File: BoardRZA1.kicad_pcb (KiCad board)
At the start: 4 copper layers, 99.9 x 80 mm, 153 parts, among them CON1 USB-MINI-B, CON2 USB-A-PCB, CON3 microSD, CON4 BARREL_JACK, J1 HR911105A, J2 SIL38, P1 JTAG, SW1 RESET, SW2 NMI, SW3 SW0, SW4 SW1, U1 RZ-A1L, U2 13MHz, U3 48MHz, U4 N25QXXX, U5 AS4C16M16S, U6 BA3259HFP, U7 BU42xx, U8 KSZ8041MLL, U9 25MHz, X1 32.768k

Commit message: Logo & move some nets
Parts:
- added SYM: Symbol_OSHW-Logo_CopperTop_07Jul2012, Symbols:Symbol_OSHW-Logo_CopperTop, F.Cu at (28.5, 79.1)
- added SYM: Symbol_OSHW-Logo_CopperTop_07Jul2012, Symbols:Symbol_OSHW-Logo_CopperTop, B.Cu at (103.0, 86.1)
- added Sym: Symbol_ESD-Logo_CopperTop_21Apr2011, Symbols:Symbol_ESD-Logo_CopperTop, F.Cu at (31.3, 72.3)
- added Sym: Symbol_CreativeCommons_Typ2_CopperTop_Small, Symbols:Symbol_CreativeCommons_CopperTop_Type2_Small, F.Cu at (34.3, 79.1)
- added Sym: Symbol_CreativeCommons_Typ2_CopperTop_Small, Symbols:Symbol_CreativeCommons_CopperTop_Type2_Small, B.Cu at (96.9, 86.0)
- added Sym: Symbol_ESD-Logo_CopperTop_21Apr2011, Symbols:Symbol_ESD-Logo_CopperTop, B.Cu at (99.8, 78.4)
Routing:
- net VSS: track 590.2 -> 559.9 mm, vias 38 -> 41
- net Net-(CON1-Pad1): track 51.0 -> 60.8 mm
- net /ET_TXD2: track 82.8 -> 84.7 mm
- net /ET_TXD1: track 82.0 -> 83.9 mm
- net /ET_TXD0: track 83.0 -> 85.0 mm
- net /ET_TXD3: track 85.3 -> 87.2 mm
- net /ET_TXCLK: track 68.1 -> 70.0 mm
- net /P6_8: track 117.9 -> 116.7 mm
- net /SW0: track 43.9 -> 42.7 mm
- net /P6_7: track 128.6 -> 127.5 mm
- added copper zone on B.Cu, net /ET_1v8

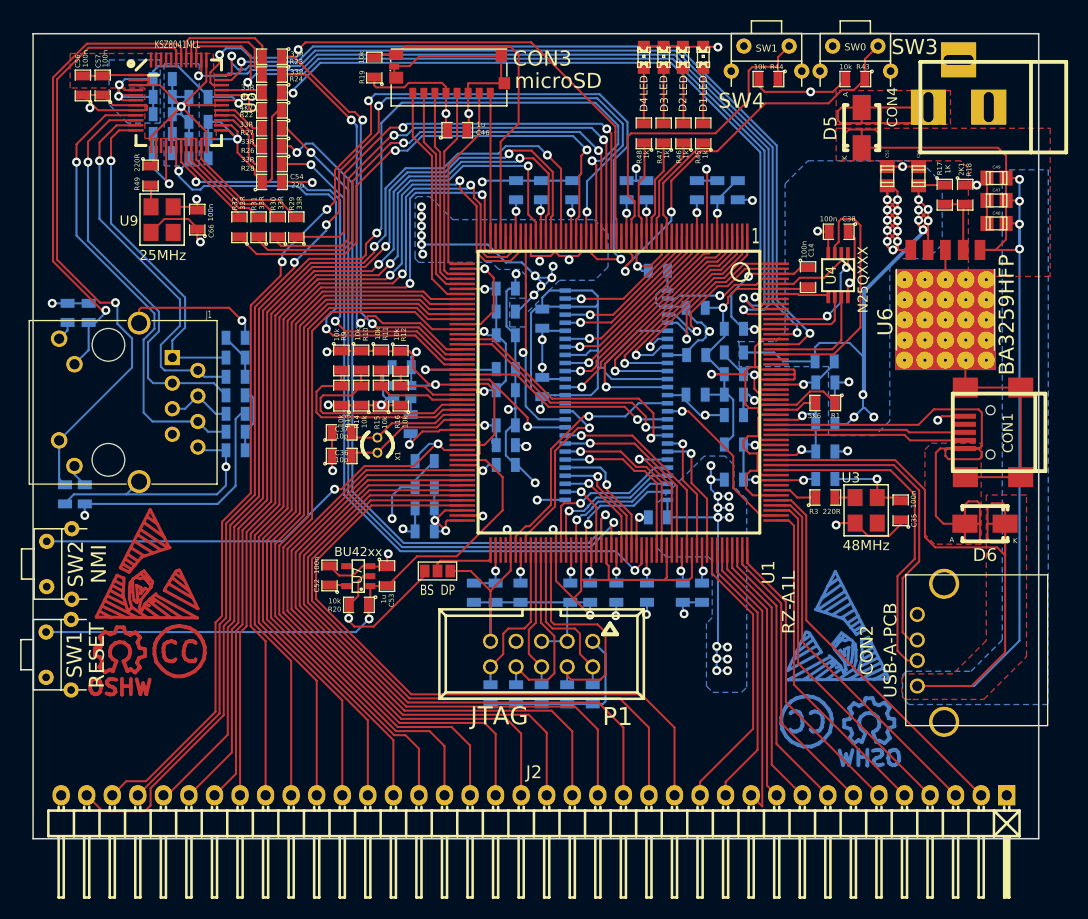
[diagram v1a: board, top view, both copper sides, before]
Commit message: PHY OSC to XI fixed. Move some refs. Optional pulldown on TRST
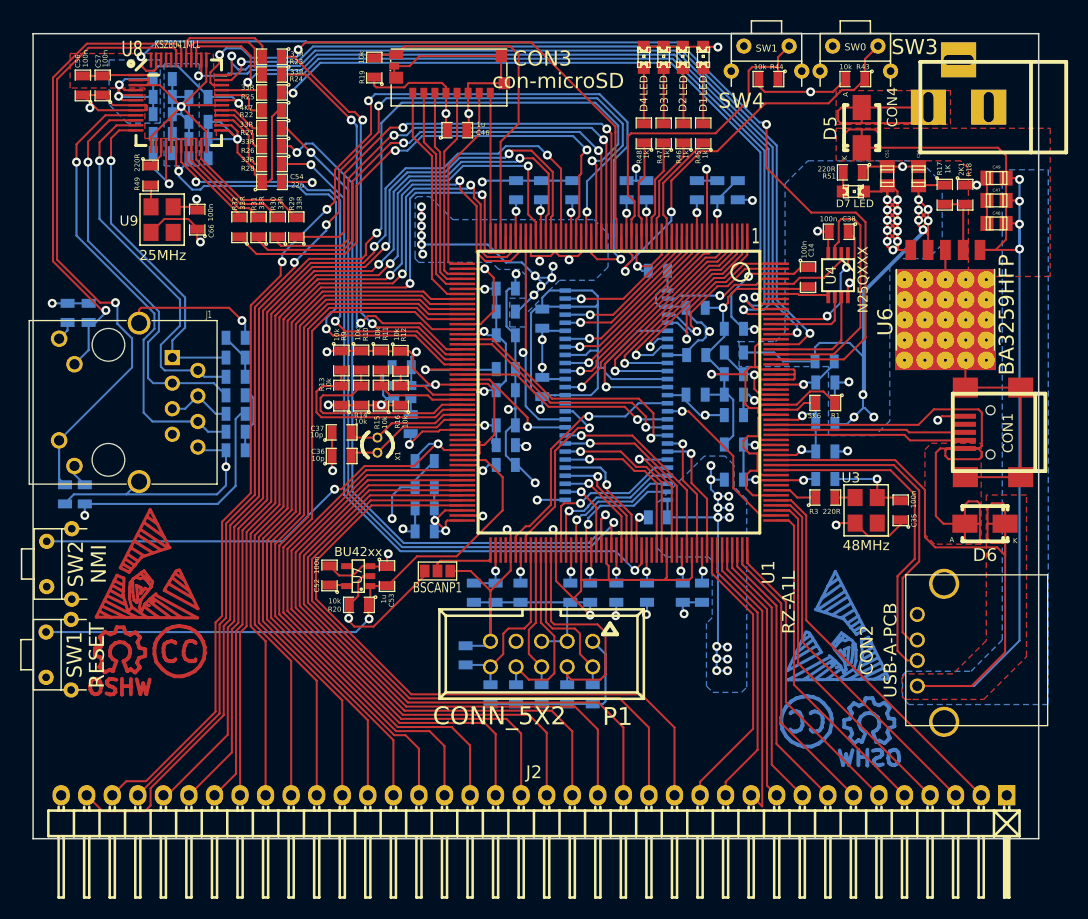
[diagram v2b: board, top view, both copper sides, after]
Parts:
- removed BS  DP: GS3, Connect:GS3
- added BSCANP1: GS3, Connect:GS3, F.Cu at (60.1, 71.0)
- added D7: LED, LEDs:LED-0805, F.Cu at (101.4, 33.3)
- added R50: 10k, SMD_Packages:SM0805, B.Cu at (62.9, 79.4)
- added R51: 220R, SMD_Packages:SM0805, F.Cu at (101.3, 31.4)
- CON3: value microSD -> con-microSD
- P1: value JTAG -> CONN_5X2
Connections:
- U1 pad 189: Net-(U1-Pad189) -> /PHY_RESET
- U8 pad 14: /ETH_CLK -> Net-(U8-Pad14)
- U8 pad 15: Net-(U8-Pad15) -> /ETH_CLK
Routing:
- net /PHY_RESET: track 0.00 -> 107.5 mm, vias 0 -> 2
- net VSS: track 559.9 -> 565.2 mm
- net /JTAG_TRST: track 16.0 -> 18.5 mm
- net +3.3V: track 317.7 -> 320.2 mm
- net Net-(D7-Pad1): track 0.00 -> 1.92 mm

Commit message: Add 10uF decouple on pvcc, vcc & 3v3
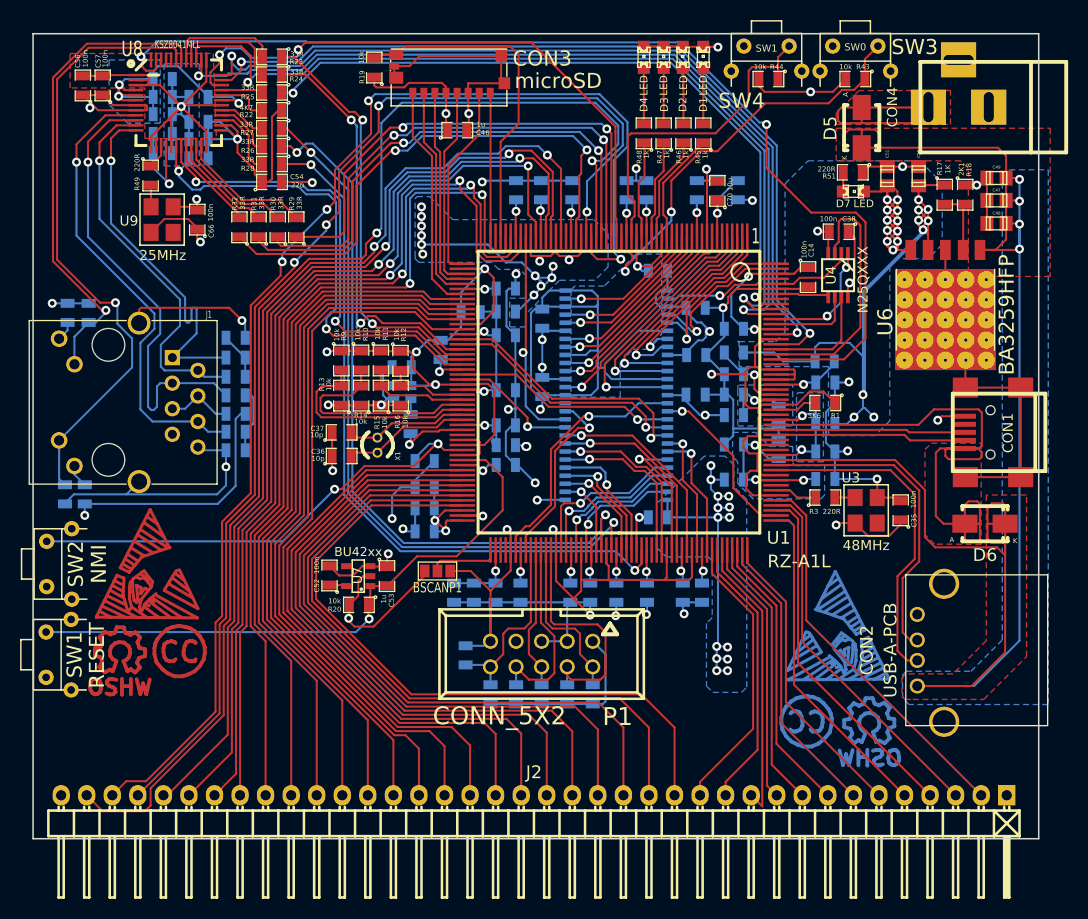
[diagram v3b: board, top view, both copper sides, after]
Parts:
- added C67: 10u, SMD_Packages:SM0805, B.Cu at (94.0, 55.6)
- added C68: 10u, SMD_Packages:SM0805, B.Cu at (94.0, 58.9)
- added C69: 10u, SMD_Packages:SM0805, B.Cu at (63.4, 45.3)
- added C70: 10u, SMD_Packages:SM0805, F.Cu at (87.9, 33.2)
- added C71: 10u, SMD_Packages:SM0805, B.Cu at (61.7, 73.2)
- CON3: value con-microSD -> microSD
- moved C17 6.75 mm to (60.4, 49.0), turned to 90 degrees
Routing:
- net VSS: track 565.2 -> 594.8 mm
- net /VCC: track 131.8 -> 126.0 mm
- net Net-(J1-Pad3): track 41.5 -> 46.7 mm
- net Net-(J1-Pad1): track 33.5 -> 37.6 mm
- net /USBDPVCC: track 14.0 -> 16.9 mm
- net /PVCC: track 176.3 -> 179.1 mm
- net /USBAPVCC: track 5.54 -> 8.19 mm
- added copper zone on B.Cu, net /USBAPVCC
- added copper zone on B.Cu, net /USBDPVCC
- added copper zone on B.Cu, net /USBDVCC

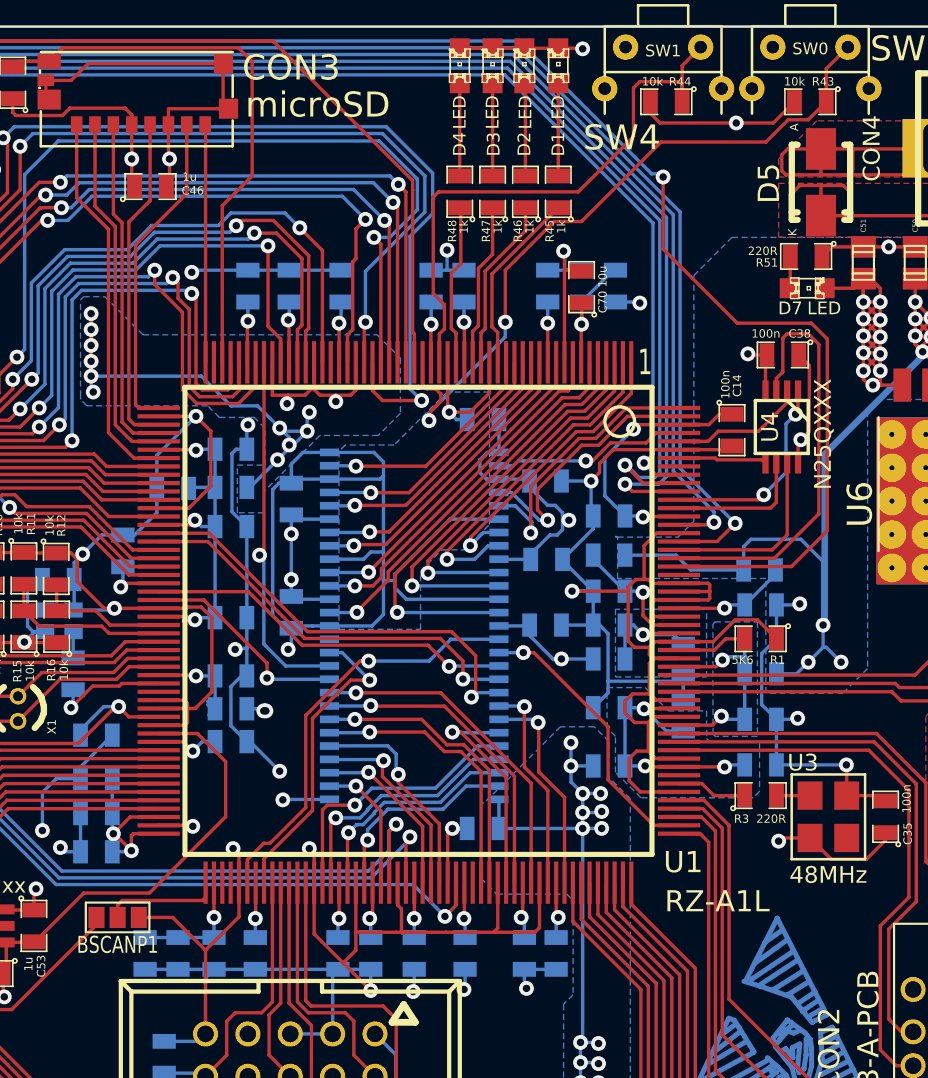
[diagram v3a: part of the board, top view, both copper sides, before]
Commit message: Add 100pF C over power rails (700MHz filters) ERC pass DRC pass
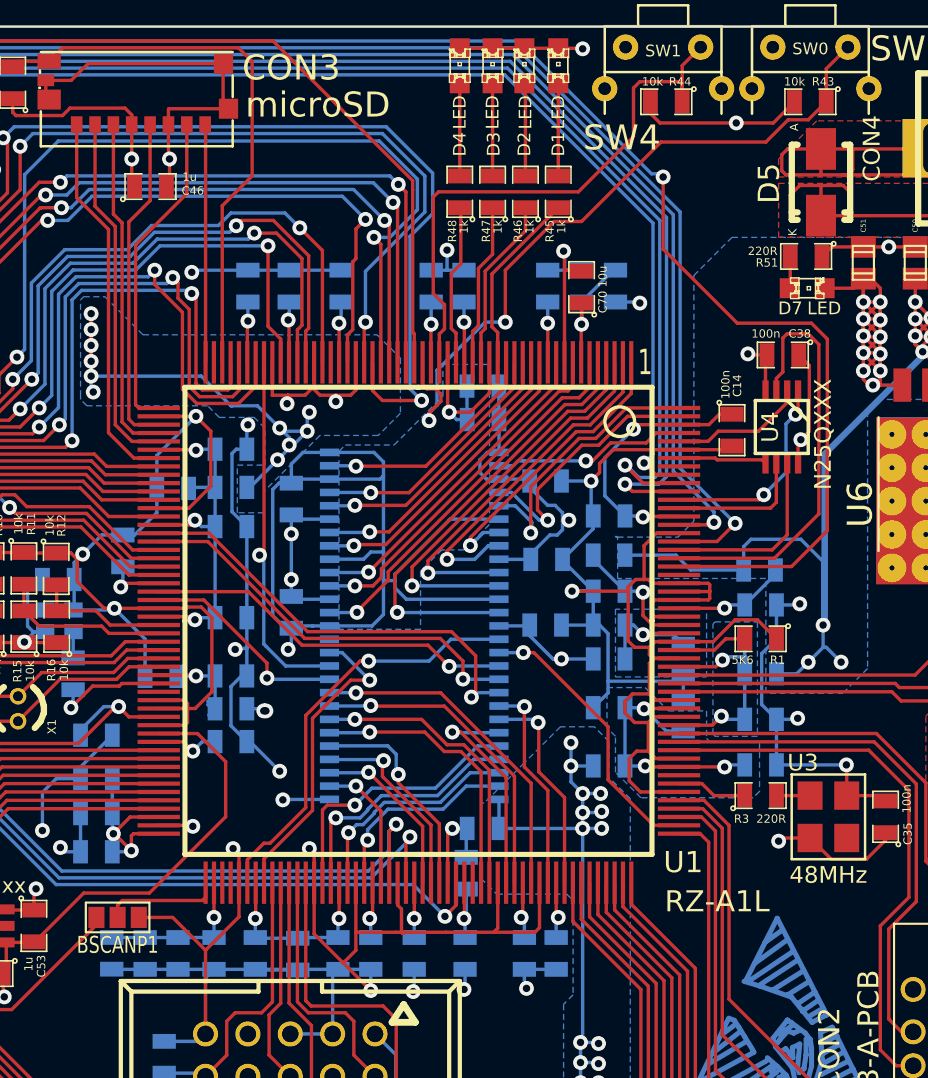
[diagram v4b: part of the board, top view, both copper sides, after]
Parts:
- added C72: 100p, SMD_Packages:SM0805, B.Cu at (82.0, 39.1)
- added C73: 100p, SMD_Packages:SM0805, B.Cu at (81.0, 68.3)
- added C74: 100p, SMD_Packages:SM0805, B.Cu at (59.7, 73.1)
- added C75: 100p, SMD_Packages:SM0805, B.Cu at (70.9, 73.2)
- added C76: 100p, SMD_Packages:SM0805, B.Cu at (62.7, 56.5)
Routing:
- net VSS: track 594.8 -> 608.0 mm
- net /VCC: track 126.0 -> 131.0 mm
- net /PVCC: track 179.1 -> 183.0 mm
- net +3.3V: track 320.2 -> 322.2 mm
- net /PLLVCC: track 7.62 -> 8.78 mm
- net /SW0: track 42.7 -> 43.4 mm

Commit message: Arrangue PCB
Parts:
- moved R20 9.11 mm to (60.9, 71.4), turned to 90 degrees
- moved C52 7.15 mm to (55.9, 68.6), turned to 0 degrees
- moved BSCANP1 4.47 mm to (64.1, 73.0)
- moved SYM 4.31 mm to (100.1, 82.9)
- moved C53 3.87 mm to (58.9, 71.4)
- moved Sym 3.85 mm to (94.8, 82.8)
- moved U7 3.68 mm to (55.9, 71.3)
- moved Sym 3.56 mm to (97.0, 76.3)
- moved SYM 3.51 mm to (31.7, 77.6)
- moved Sym 3.44 mm to (34.5, 71.0)
- moved Sym 3.30 mm to (37.3, 77.6)
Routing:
- net VSS: track 608.0 -> 600.6 mm, vias 41 -> 40
- net /P1_13: track 65.6 -> 59.4 mm
- net /P1_10: track 61.3 -> 55.2 mm
- net /P1_9: track 60.0 -> 53.8 mm
- net /P1_15: track 68.3 -> 62.1 mm
- net /P1_14: track 66.9 -> 60.7 mm
- net /P1_11: track 62.7 -> 56.6 mm
- net /P1_8: track 58.6 -> 52.4 mm
- net /P1_12: track 64.2 -> 58.0 mm
- net +3.3V: track 322.2 -> 327.8 mm, vias 54 -> 53
- net /P1_0: track 28.2 -> 24.9 mm
- net Net-(C52-Pad1): track 1.70 -> 4.73 mm
- net /P7_9: track 70.2 -> 67.8 mm
- net /P7_8: track 70.0 -> 67.5 mm
- net /P7_10: track 70.5 -> 68.0 mm
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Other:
- board text added: "+3.3v"
- board text added: "GND"
- board text added: "P1.0"
- board text added: "P1.1"
- board text added: "P1.10"
- board text added: "P1.11"
- board text added: "P1.12"
- board text added: "P1.13"
- board text added: "P1.14"
- board text added: "P1.15"
- board text added: "P1.2"
- board text added: "P1.3"
- board text added: "P1.4"
- board text added: "P1.5"
- board text added: "P1.6"
- board text added: "P1.7"
- board text added: "P1.8"
- board text added: "P1.9"
- board text added: "P2.7"
- board text added: "P2.8"
- board text added: "P2.9"
- board text added: "P3.15"
- board text added: "P6.10"
- board text added: "P6.11"
- board text added: "P6.12"
- board text added: "P6.13"
- board text added: "P6.14"
- board text added: "P6.15"
- board text added: "P6.6"
- board text added: "P6.7"
- board text added: "P6.9"
- board text added: "P7.10"
- board text added: "P7.11"
- board text added: "P7.12"
- board text added: "P7.13"
- board text added: "P7.8"
- board text added: "P7.9"

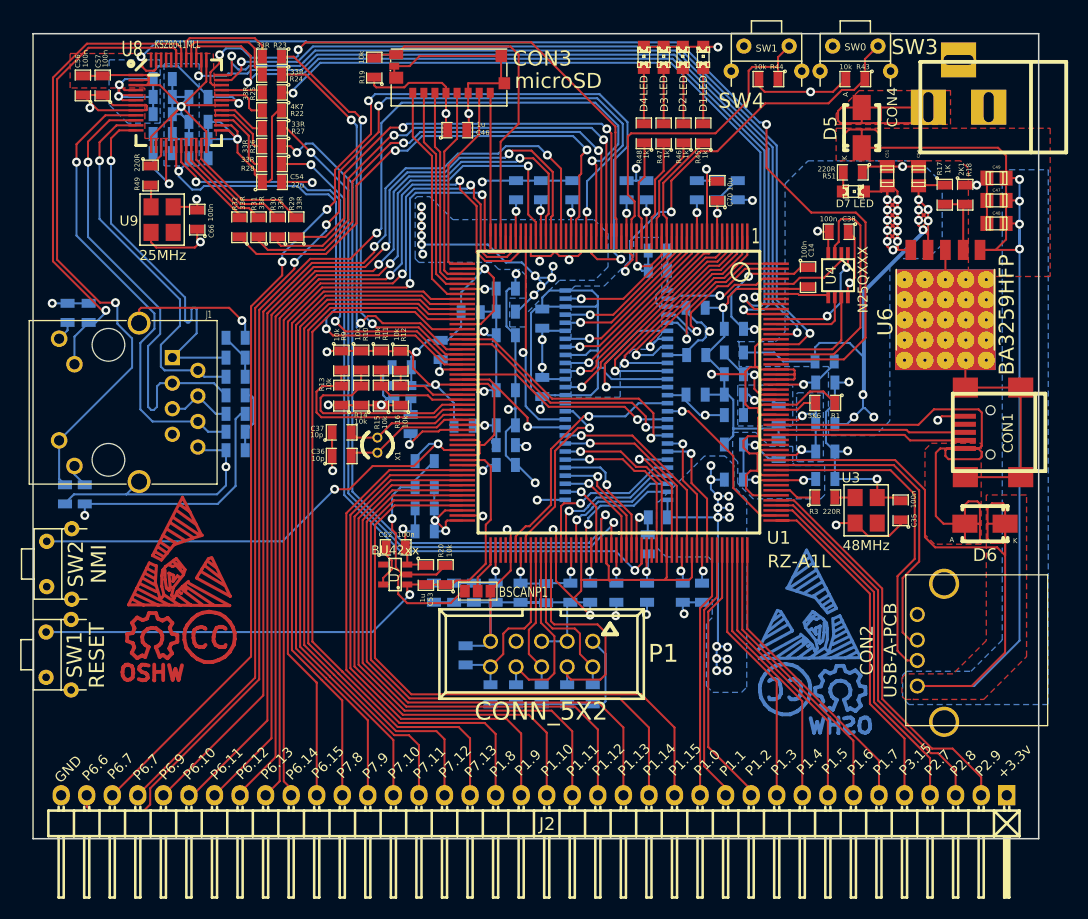
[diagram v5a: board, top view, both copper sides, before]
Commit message: Correct U4 SOP2-8 package. Rearangue footprint libraries
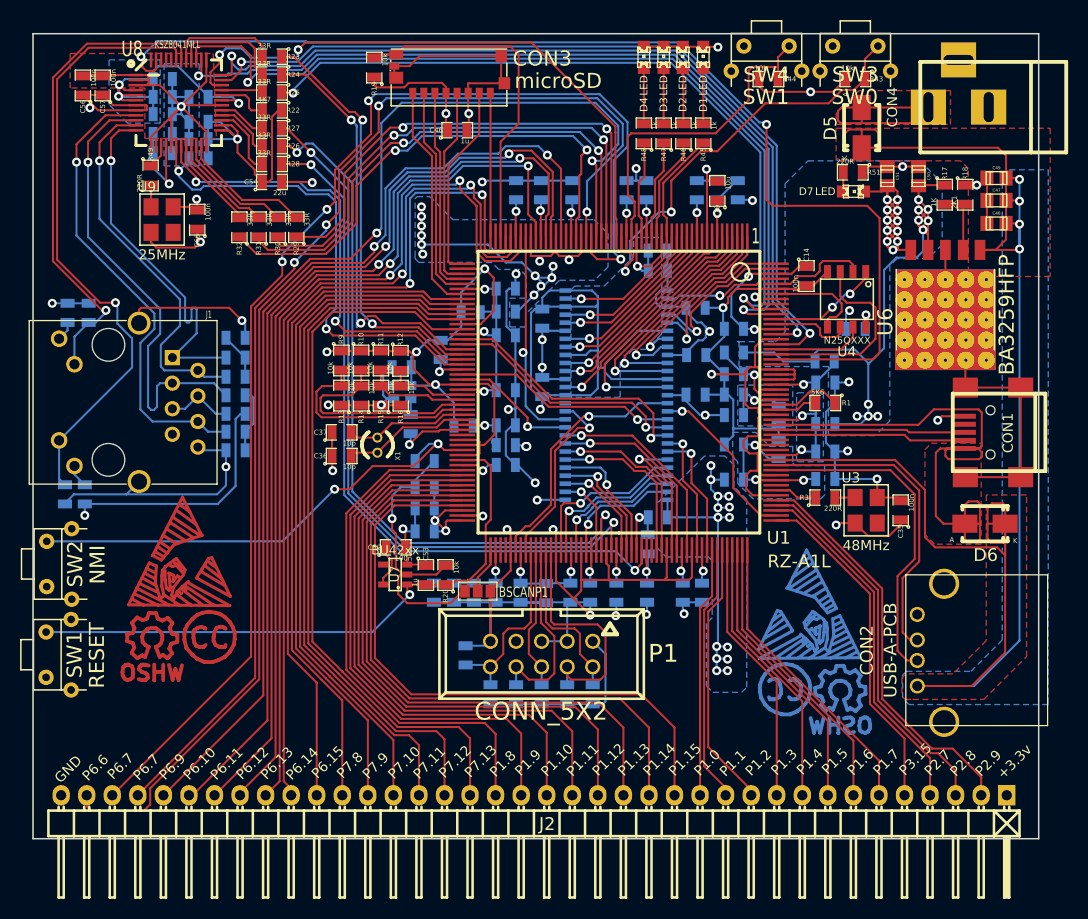
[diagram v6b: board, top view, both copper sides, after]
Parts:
- BSCANP1: footprint Connect:GS3 -> footprints:GS3
- C1, C10, C11, C12, C13, C14, C15, C16, C17, C18, C19, C2, C20, C21, C22, C23, C24, C25, C26, C27, C28, C29, C3, C30, C31, C32, C33, C34, C35, C36, C37, C39, C4, C40, C41, C42, C43, C44, C45, C46, C5, C52, C53, C54, C55, C56, C57, C58, C59, C6, C60, C61, C62, C63, C64, C65, C66, C67, C68, C69, C7, C70, C71, C72, C73, C74, C75, C76, C8, C9, L1, L10, L2, L3, L4, L5, L6, L7, L8, L9, R1, R10, R11, R12, R13, R14, R15, R16, R17, R18, R19, R2, R20, R21, R22, R23, R24, R25, R26, R27, R28, R29, R3, R30, R31, R32, R33, R34, R35, R36, R37, R38, R39, R4, R40, R41, R42, R43, R44, R45, R46, R47, R48, R49, R5, R50, R51, R6, R7, R8, R9: footprint SMD_Packages:SM0805 -> footprints:SM0805
- C38: footprint SMD_Packages:SM0805 -> footprints:SM0805; moved to B.Cu
- C47, C48, C49, C50, C51: footprint Capacitors_SMD:c_0805 -> footprints:c_0805
- CON1: footprint Connect:USB_MINI_B -> footprints:USB_MINI_B
- CON2: footprint Connect:USB_A -> footprints:USB_A
- CON3: footprint microsd:microSD -> footprints:microSD
- CON4: footprint Connect:BARREL_JACK -> footprints:BARREL_JACK
- D1, D2, D3, D4, D7: footprint LEDs:LED-0805 -> footprints:LED-0805
- D5, D6: footprint Diodes_SMD:Diode-SMA_Standard -> footprints:Diode-SMA_Standard
- J1: footprint RJ45:RJ45_Pulse_J403-A -> footprints:RJ45_Pulse_J403-A
- J2: footprint Pin_Headers:Pin_Header_Angled_1x38 -> footprints:Pin_Header_Angled_1x38
- P1: footprint Connect:VASCH5x2 -> footprints:VASCH5x2
- SW1, SW2, SW3, SW4: footprint PushButton:RigthAnglePush -> footprints:RigthAnglePush
- U1: footprint SMD_Packages:PQFP208 -> footprints:PQFP208
- U2: footprint OSC_4PIN:OSC_2x2p5 -> footprints:OSC_2x2p5
- U3, U9: footprint OSC_4PIN:OSC_4PIN -> footprints:OSC_4PIN
- U4: footprint SMD_Packages:MSOP_8 -> footprints:SOP2-8
- U5: footprint TSOP_II_54:TSOP_II_54 -> footprints:TSOP_II_54
- U6: footprint Rohm:Rohm-HRP5 -> footprints:Rohm-HRP5
- U7: footprint Rohm:SSOP-5 -> footprints:SSOP-5
- U8: footprint smd_qfp:LQFP48-M05 -> footprints:LQFP48-M05
- X1: footprint Crystals:Crystal_Round_Vertical_3mm -> footprints:Crystal_Round_Vertical_3mm
- moved C38 9.80 mm to (101.6, 46.9)
- moved U4 5.84 mm to (102.6, 46.7)
- moved C14 0.19 mm to (96.7, 41.7)
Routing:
- net +1.2V: track 86.9 -> 66.8 mm, vias 12 -> 13
- net /PHY_RESET: track 107.5 -> 113.2 mm
- net /SPBIO_20_0: track 25.5 -> 20.0 mm
- net /SPBIO_00_0: track 5.31 -> 10.2 mm
- net +3.3V: track 327.8 -> 323.4 mm
- net /SPBIO_30_0: track 11.2 -> 9.18 mm
- net /SPBIO_10_0: track 8.14 -> 9.84 mm
- net VSS: track 600.6 -> 601.8 mm
- net /SPBSSL_0: track 12.3 -> 11.3 mm
